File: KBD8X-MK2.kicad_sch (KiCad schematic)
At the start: 24 parts, among them J1 AVR-ISP-6, SW1 SW_Push, U1 ATmega32U4-MU, U2 PRTR5V0U2X, Y1 16MHz

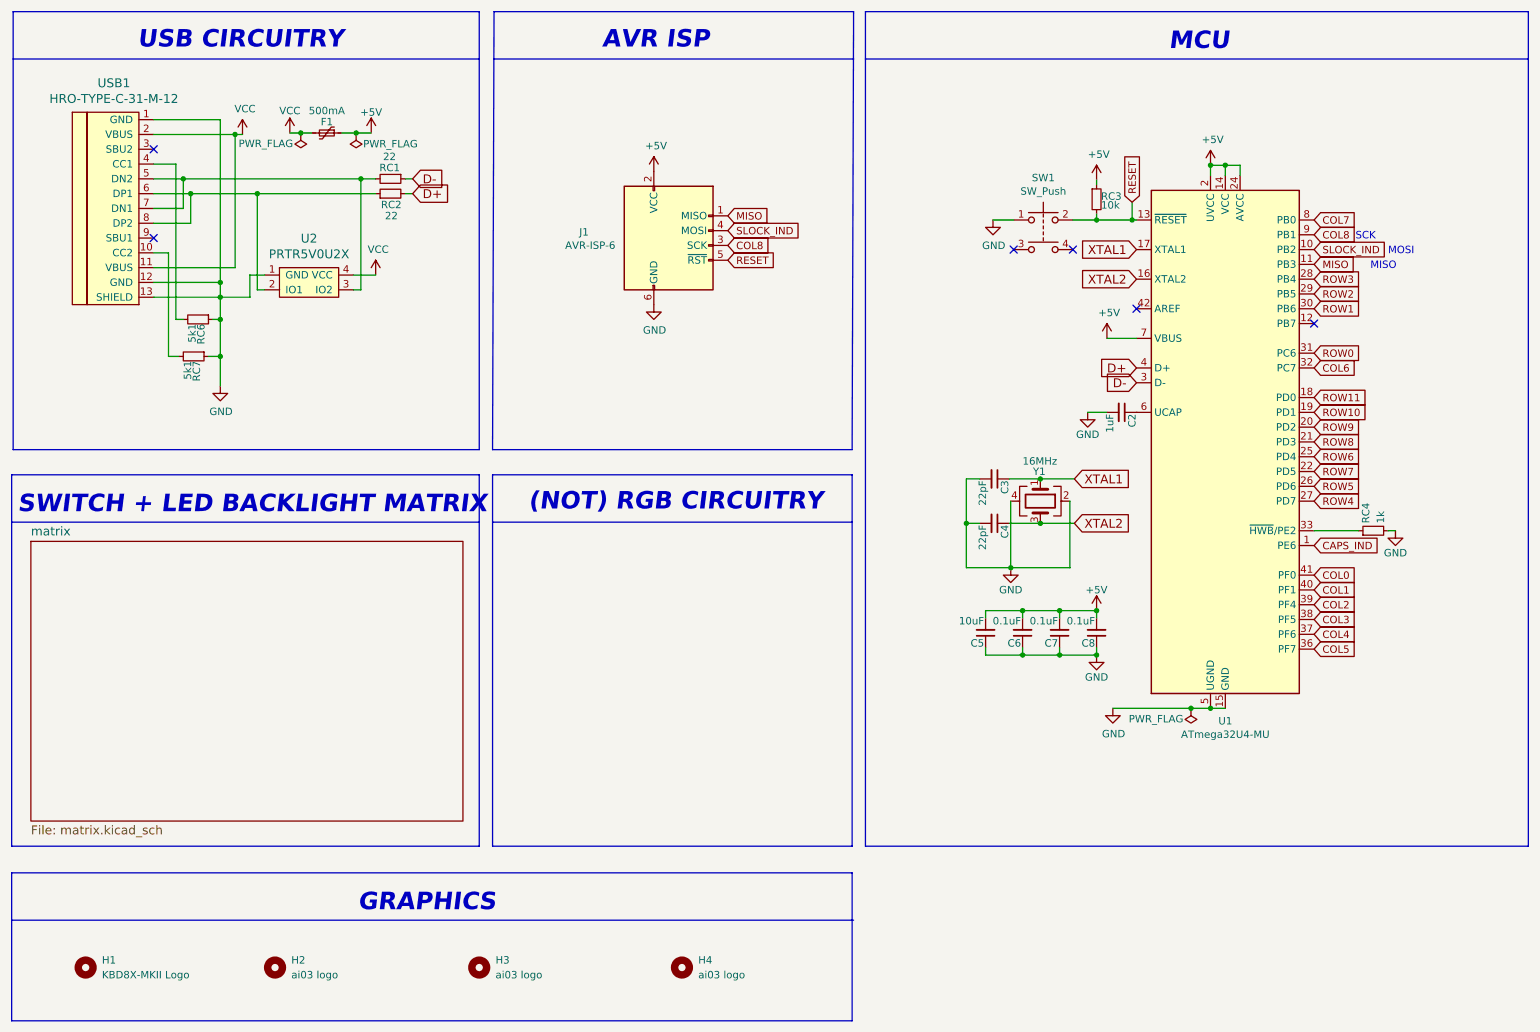
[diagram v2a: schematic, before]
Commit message: Added OLED display
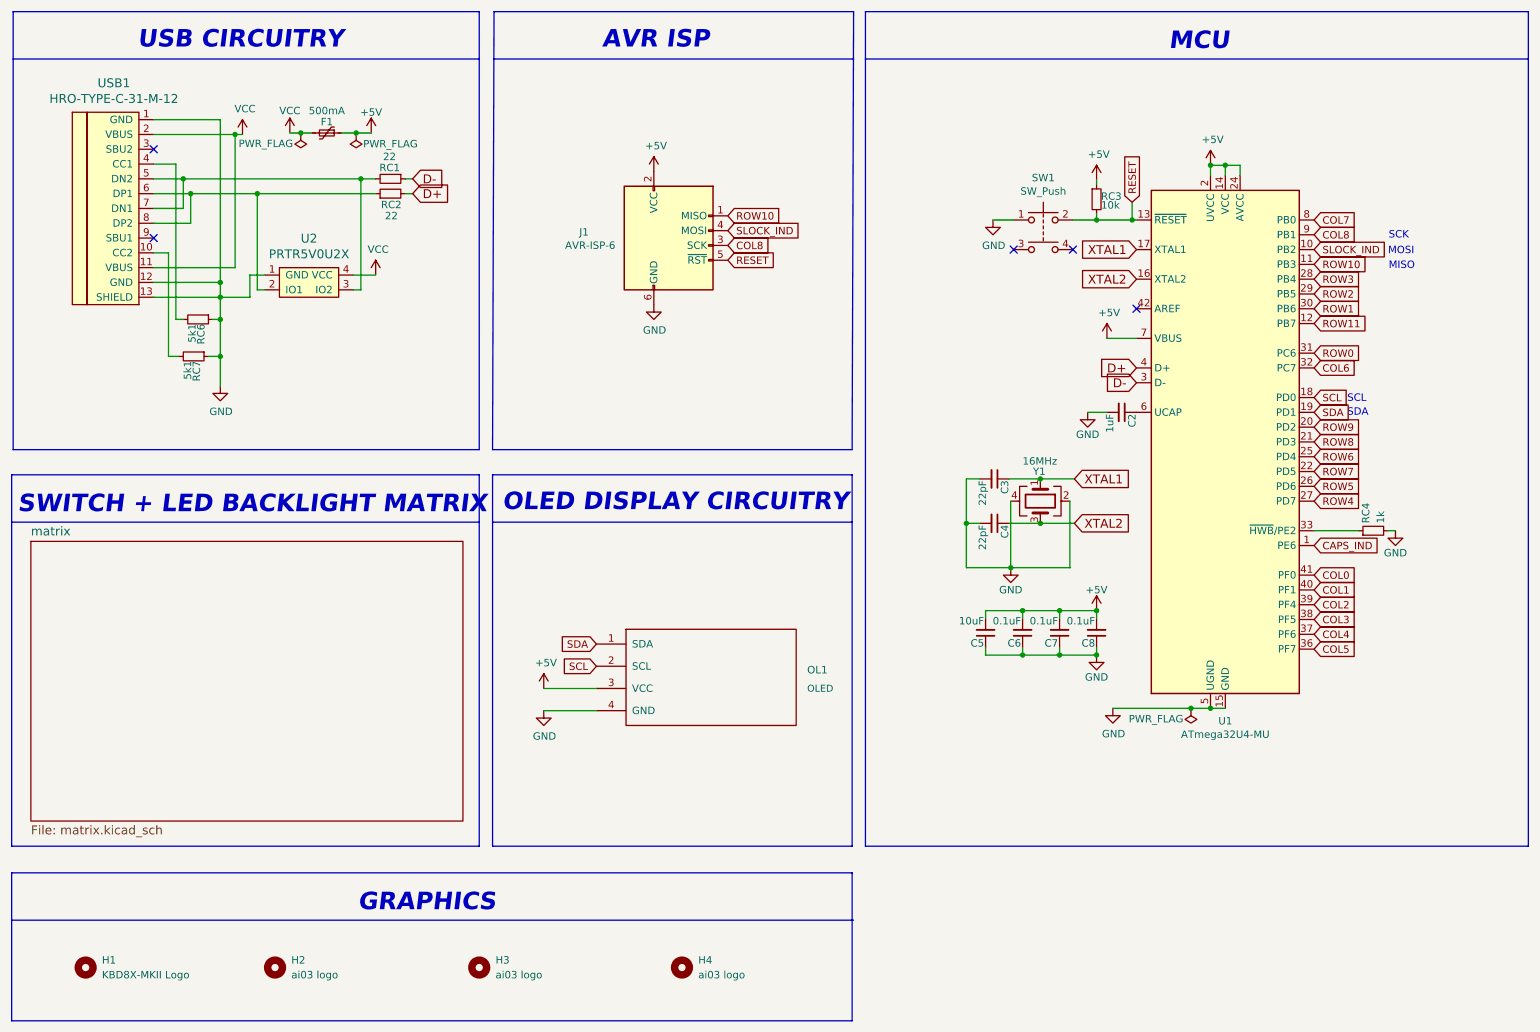
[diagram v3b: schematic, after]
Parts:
- added OL1: OLED, KBD8X_MK2_Components:OLED, symbol KBD8X_MK2_Components:OLED
- U1: footprint Package_DFN_QFN:QFN-44-1EP_7x7mm_P0.5mm_EP5.2x5.2mm -> KBD8X_MK2_Components:QFN-44-1EP_7x7mm_Pitch0.5mm
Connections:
- net MISO is gone; now on net ROW10: J1.1 (MISO), U1.11 (PB3)
- net +5V: now also OL1.3 (VCC)
- net GND: now also OL1.4 (GND)
- net ROW10: no longer U1.19 (PD1)
- net ROW11: now also U1.12 (PB7); no longer U1.18 (PD0)
- new net SCL: OL1.2 (SCL), U1.18 (PD0)
- new net SDA: OL1.1 (SDA), U1.19 (PD1)
- no-connect marks 6 -> 5
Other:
- note added: "OLED DISPLAY CIRCUITRY"
- note added: "SCL"
- note added: "SDA"
- note removed: "(NOT) RGB CIRCUITRY"
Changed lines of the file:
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@@
   (no_connect (at 42.164 57.15))
   (no_connect (at 210.8708 69.2912))
-  (no_connect (at 241.3508 71.8312))
   (wire (pts (xy 67.4116 39.116) (xy 69.342 39.116))
     (stroke (width 0) (type default) (color 0 0 0 0))
@@
     (stroke (width 0) (type default) (color 0 0 0 0))
   )
+  (wire (pts (xy 109.1184 138.2776) (xy 118.1608 138.2776))
+    (stroke (width 0) (type default) (color 0 0 0 0))
+  )
   (wire (pts (xy 204.0128 53.0352) (xy 204.0128 54.0512))
     (stroke (width 0) (type default) (color 0 0 0 0))
@@
     (stroke (width 0) (type default) (color 0 0 0 0))
   )
+  (wire (pts (xy 109.1184 134.4676) (xy 118.1608 134.4676))
+    (stroke (width 0) (type default) (color 0 0 0 0))
+  )
   (wire (pts (xy 204.0128 128.7272) (xy 204.0128 127.4572))
     (stroke (width 0) (type default) (color 0 0 0 0))
@@
     (stroke (width 0) (type default) (color 0 0 0 0))
   )
-  (text "SCK" (at 248.4628 57.6072 0)
+  (text "SDA" (at 247.0404 87.884 0)
+    (effects (font (size 1.27 1.27)) (justify left bottom))
+  )
+  (text "SCK" (at 254.1524 57.4548 0)
     (effects (font (size 1.27 1.27)) (justify left bottom))
   )
@@
     (effects (font (size 3 3) (thickness 1.4) bold italic) (justify left bottom))
   )
-  (text "(NOT) RGB CIRCUITRY" (at 106.4768 104.1908 0)
+  (text "OLED DISPLAY CIRCUITRY" (at 102.0064 104.2924 0)
     (effects (font (size 3 3) (thickness 1.4) bold italic) (justify left bottom))
   )
@@
     (effects (font (size 3 3) (thickness 1.4) bold italic) (justify left bottom))
   )
+  (text "SCL" (at 247.0404 85.4964 0)
+    (effects (font (size 1.27 1.27)) (justify left bottom))
+  )
   (text "MOSI" (at 254.0508 60.1472 0)
     (effects (font (size 1.27 1.27)) (justify left bottom))
@@
     (effects (font (size 3 3) (thickness 1.4) bold italic) (justify left bottom))
   )
-  (text "MISO" (at 251.0028 62.6872 0)
+  (text "MISO" (at 254.1524 62.6872 0)
     (effects (font (size 1.27 1.27)) (justify left bottom))
   )
@@
     )
   )
-  (global_label "ROW11" (shape input) (at 241.3508 84.5312 0) (fields_autoplaced)
-    (effects (font (size 1.27 1.27)) (justify left))
-    (property "Intersheet References" "${INTERSHEET_REFS}" (id 0) (at 104.1908 -36.1188 0)
+  (global_label "ROW11" (shape input) (at 241.3508 71.8312 0) (fields_autoplaced)
+    (effects (font (size 1.27 1.27)) (justify left))
+    (property "Intersheet References" "${INTERSHEET_REFS}" (id 0) (at 104.1908 -48.8188 0)
       (effects (font (size 1.27 1.27)) hide)
     )
@@
     )
   )
-  (global_label "ROW10" (shape input) (at 241.3508 87.0712 0) (fields_autoplaced)
-    (effects (font (size 1.27 1.27)) (justify left))
-    (property "Intersheet References" "${INTERSHEET_REFS}" (id 0) (at 104.1908 -36.1188 0)
+  (global_label "ROW10" (shape input) (at 241.3508 61.6712 0) (fields_autoplaced)
+    (effects (font (size 1.27 1.27)) (justify left))
+    (property "Intersheet References" "${INTERSHEET_REFS}" (id 0) (at 104.1908 -61.5188 0)
       (effects (font (size 1.27 1.27)) hide)
     )
@@
     )
   )
-  (global_label "MISO" (shape input) (at 140.716 53.34 0) (fields_autoplaced)
-    (effects (font (size 1.27 1.27)) (justify left))
-    (property "Intersheet References" "${INTERSHEET_REFS}" (id 0) (at 147.6364 53.2606 0)
+  (global_label "SCL" (shape input) (at 118.1608 130.6576 180) (fields_autoplaced)
+    (effects (font (size 1.27 1.27)) (justify right))
+    (property "Intersheet References" "${INTERSHEET_REFS}" (id 0) (at 112.329 130.5782 0)
+      (effects (font (size 1.27 1.27)) (justify right) hide)
+    )
+  )
+  (global_label "ROW10" (shape input) (at 140.716 53.34 0) (fields_autoplaced)
+    (effects (font (size 1.27 1.27)) (justify left))
+    (property "Intersheet References" "${INTERSHEET_REFS}" (id 0) (at 149.5112 53.2606 0)
+      (effects (font (size 1.27 1.27)) (justify left) hide)
+    )
+  )
+  (global_label "SCL" (shape input) (at 241.3508 84.5312 0) (fields_autoplaced)
+    (effects (font (size 1.27 1.27)) (justify left))
+    (property "Intersheet References" "${INTERSHEET_REFS}" (id 0) (at 247.1826 84.6106 0)
       (effects (font (size 1.27 1.27)) (justify left) hide)
     )
@@
     )
   )
-  (global_label "MISO" (shape input) (at 241.3508 61.6712 0) (fields_autoplaced)
-    (effects (font (size 1.27 1.27)) (justify left))
-    (property "Intersheet References" "${INTERSHEET_REFS}" (id 0) (at 248.2712 61.5918 0)
+  (global_label "SDA" (shape input) (at 118.1608 126.8476 180) (fields_autoplaced)
+    (effects (font (size 1.27 1.27)) (justify right))
+    (property "Intersheet References" "${INTERSHEET_REFS}" (id 0) (at 112.2685 126.7682 0)
+      (effects (font (size 1.27 1.27)) (justify right) hide)
+    )
+  )
+  (global_label "COL0" (shape input) (at 241.3508 115.0112 0) (fields_autoplaced)
+    (effects (font (size 1.27 1.27)) (justify left))
+    (property "Intersheet References" "${INTERSHEET_REFS}" (id 0) (at 104.1908 -36.1188 0)
+      (effects (font (size 1.27 1.27)) hide)
+    )
+  )
+  (global_label "SDA" (shape input) (at 241.3508 87.0712 0) (fields_autoplaced)
+    (effects (font (size 1.27 1.27)) (justify left))
+    (property "Intersheet References" "${INTERSHEET_REFS}" (id 0) (at 247.2431 87.1506 0)
       (effects (font (size 1.27 1.27)) (justify left) hide)
-    )
-  )
-  (global_label "COL0" (shape input) (at 241.3508 115.0112 0) (fields_autoplaced)
-    (effects (font (size 1.27 1.27)) (justify left))
-    (property "Intersheet References" "${INTERSHEET_REFS}" (id 0) (at 104.1908 -36.1188 0)
-      (effects (font (size 1.27 1.27)) hide)
     )
   )
@@
     (property "Reference" "U1" (id 0) (at 226.1108 140.0556 0))
     (property "Value" "ATmega32U4-MU" (id 1) (at 226.1108 142.367 0))
-    (property "Footprint" "Package_DFN_QFN:QFN-44-1EP_7x7mm_P0.5mm_EP5.2x5.2mm" (id 2) (at 226.1108 92.1512 0)
+    (property "Footprint" "KBD8X_MK2_Components:QFN-44-1EP_7x7mm_Pitch0.5mm" (id 2) (at 226.1108 92.1512 0)
       (effects (font (size 1.27 1.27) italic) hide)
     )
@@
     (pin "2")
   )
+  (symbol (lib_id "power:GND") (at 109.1184 138.2776 0) (unit 1)
+    (in_bom yes) (on_board yes)
+    (property "Reference" "#PWR0107" (id 0) (at 109.1184 144.6276 0)
+      (effects (font (size 1.27 1.27)) hide)
+    )
+    (property "Value" "GND" (id 1) (at 109.2454 142.6718 0))
+    (property "Footprint" "" (id 2) (at 109.1184 138.2776 0)
+      (effects (font (size 1.27 1.27)) hide)
+    )
+    (property "Datasheet" "" (id 3) (at 109.1184 138.2776 0)
+      (effects (font (size 1.27 1.27)) hide)
+    )
+    (pin "1")
+  )
+  (symbol (lib_id "power:+5V") (at 109.1184 134.4676 0) (unit 1)
+    (in_bom yes) (on_board yes)
+    (property "Reference" "#PWR0108" (id 0) (at 109.1184 138.2776 0)
+      (effects (font (size 1.27 1.27)) hide)
+    )
+    (property "Value" "+5V" (id 1) (at 109.4994 130.0734 0))
+    (property "Footprint" "" (id 2) (at 109.1184 134.4676 0)
+      (effects (font (size 1.27 1.27)) hide)
+    )
+    (property "Datasheet" "" (id 3) (at 109.1184 134.4676 0)
+      (effects (font (size 1.27 1.27)) hide)
+    )
+    (pin "1")
+  )
   (symbol (lib_id "Mechanical:MountingHole") (at 30.48 182.372 0) (unit 1)
     (in_bom yes) (on_board yes) (fields_autoplaced)
@@
     )
     (pin "1")
+  )
+  (symbol (lib_id "KBD8X_MK2_Components:OLED") (at 137.2108 133.1976 0) (unit 1)
+    (in_bom yes) (on_board yes) (fields_autoplaced)
+    (property "Reference" "OL1" (id 0) (at 154.3304 131.2926 0)
+      (effects (font (size 1.2954 1.2954)) (justify left))
+    )
+    (property "Value" "OLED" (id 1) (at 154.3304 134.4676 0)
+      (effects (font (size 1.1938 1.1938)) (justify left))
+    )
+    (property "Footprint" "KBD8X_MK2_Components:OLED" (id 2) (at 137.2108 130.6576 0)
+      (effects (font (size 1.524 1.524)) hide)
+    )
+    (property "Datasheet" "" (id 3) (at 137.2108 130.6576 0)
+      (effects (font (size 1.524 1.524)) hide)
+    )
+    (pin "1")
+    (pin "2")
+    (pin "3")
+    (pin "4")
   )
   (symbol (lib_id "Mechanical:MountingHole") (at 132.842 182.372 0) (unit 1)
@@
       (reference "#PWR0106") (unit 1) (value "GND") (footprint "")
     )
+    (path "/332867b2-3be3-4674-b436-1bcb7b34df15"
+      (reference "#PWR0107") (unit 1) (value "GND") (footprint "")
+    )
+    (path "/3c93455f-7d82-4396-87b2-b351144a48d3"
+      (reference "#PWR0108") (unit 1) (value "+5V") (footprint "")
+    )
     (path "/00000000-0000-0000-0000-0000618cb8ba"
       (reference "#PWR0145") (unit 1) (value "GND") (footprint "")
@@
       (reference "MX_`1") (unit 1) (value "MX-NoLED") (footprint "KBD8X_MK2_Switches:MXOnly-1U-NoLED")
     )
+    (path "/f54301a6-e34e-4c8a-a6fe-2b7d44893692"
+      (reference "OL1") (unit 1) (value "OLED") (footprint "KBD8X_MK2_Components:OLED")
+    )
     (path "/00000000-0000-0000-0000-00005a286589/00000000-0000-0000-0000-0000642149ca"
       (reference "R32") (unit 1) (value "1k") (footprint "KBD8X_MK2_Components:R_0603")
@@
     )
     (path "/00000000-0000-0000-0000-0000618b6d6d"
-      (reference "U1") (unit 1) (value "ATmega32U4-MU") (footprint "Package_DFN_QFN:QFN-44-1EP_7x7mm_P0.5mm_EP5.2x5.2mm")
+      (reference "U1") (unit 1) (value "ATmega32U4-MU") (footprint "KBD8X_MK2_Components:QFN-44-1EP_7x7mm_Pitch0.5mm")
     )
     (path "/00000000-0000-0000-0000-00005be1fa08"
